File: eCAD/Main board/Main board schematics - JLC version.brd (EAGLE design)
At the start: 83.8 x 105.1 mm, 65 parts, among them IC1 ESP32-WROOM-32E_M113EH3200PH3Q, IC2 TP4056X, IC3 DW01A-G, IC4 ME6211C33M5G-N, IC5 ME6211C33M5G-N, Q1 IRF7319TRPBF, Q2 IRF7319TRPBF, Q3 SI2347DS-T1-GE3, Q4 FS8205A, U1 ARDUINOR3-BPLACE

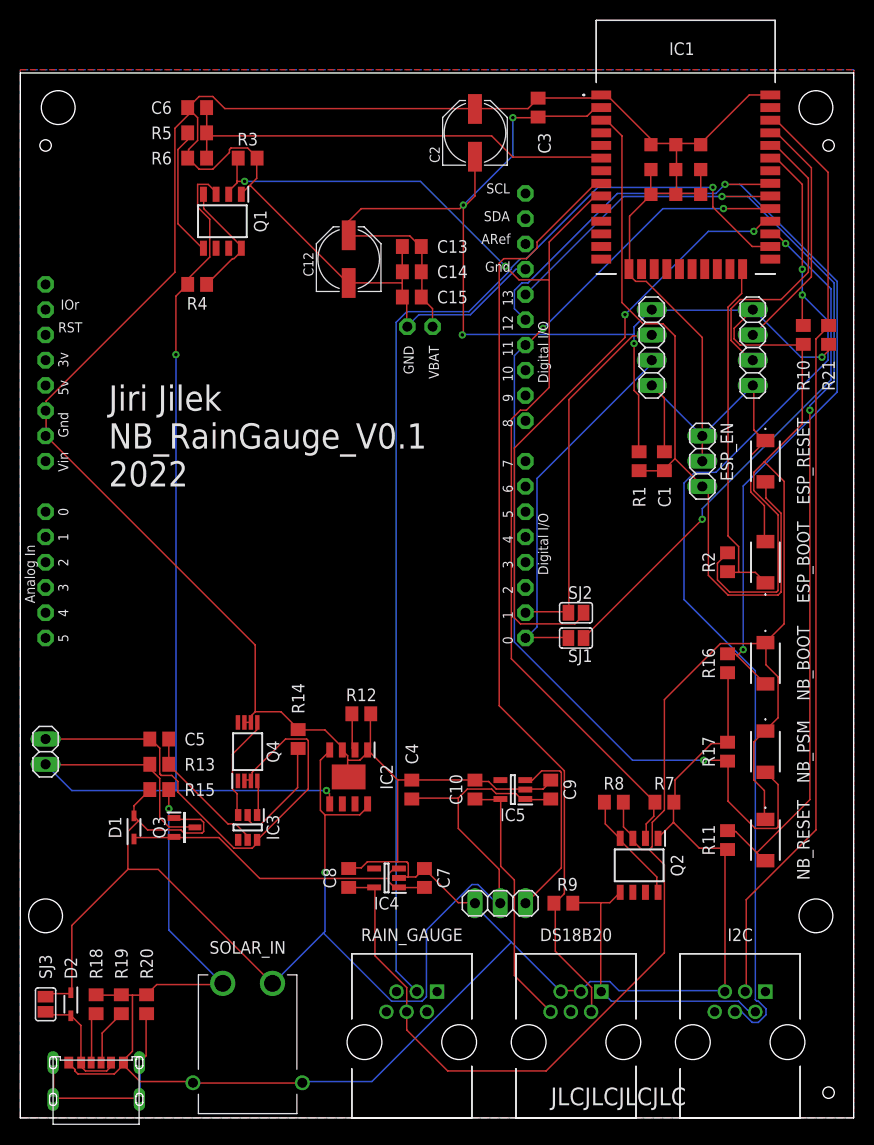
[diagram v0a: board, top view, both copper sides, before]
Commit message: Repair mistakes: C2, flash pin on ESP, fan pinout
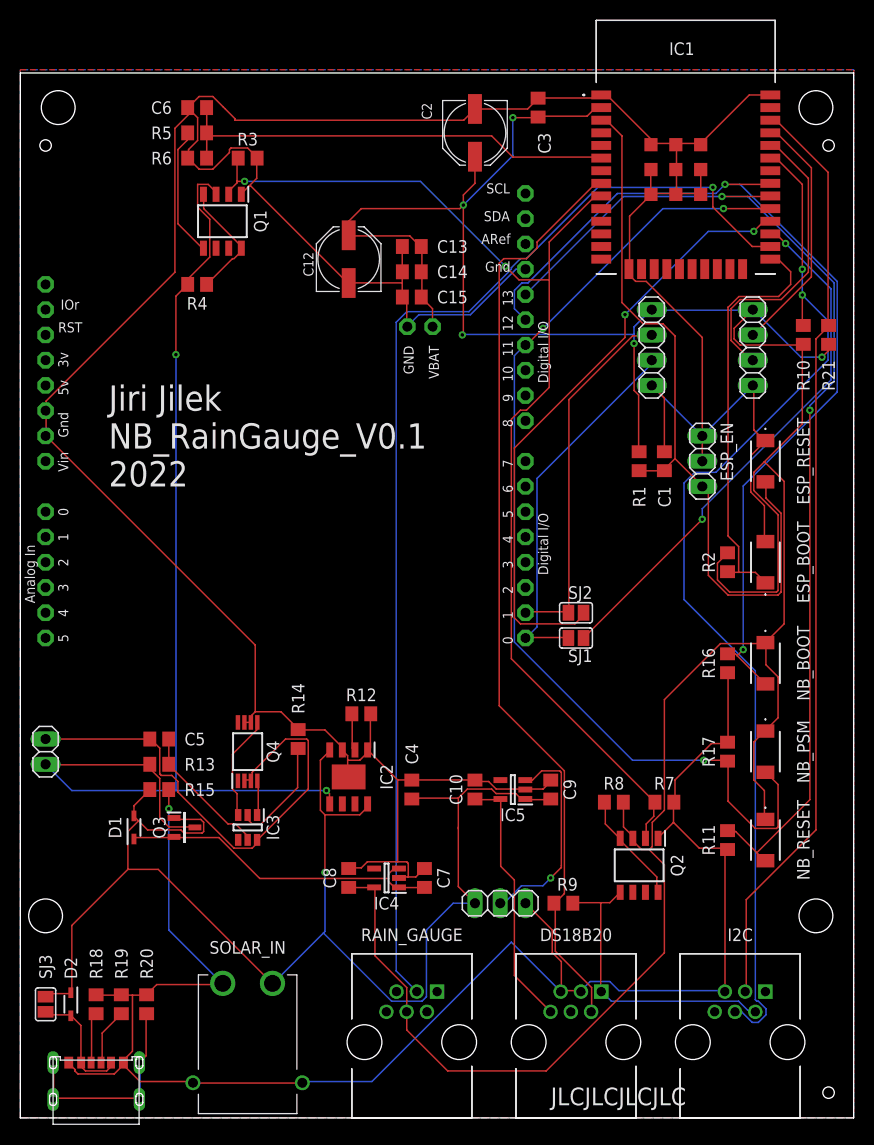
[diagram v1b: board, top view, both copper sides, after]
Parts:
- turned C2 to 270 degrees
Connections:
- net ESP_FLASH: now also IC1.25; no longer IC1.24
- net GND: now also C2.-, FAN.1; no longer C2.+, FAN.3
- net N$6: now also FAN.2; no longer FAN.1
- net VDD33: now also C2.+; no longer C2.-
- net VIN: now also FAN.3; no longer FAN.2
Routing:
- net ESP_FLASH: track 35.9 -> 42.5 mm
- net VIN: track 145.9 -> 140.8 mm
- net N$6: track 18.7 -> 21.3 mm, vias 0 -> 1
- net GND: track 522.2 -> 521.6 mm
